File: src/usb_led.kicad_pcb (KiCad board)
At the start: 2 copper layers, 22.2 x 11.4 mm, 6 parts, among them J1 HX TYPE-C 6PIN, SW1 BTN_ON

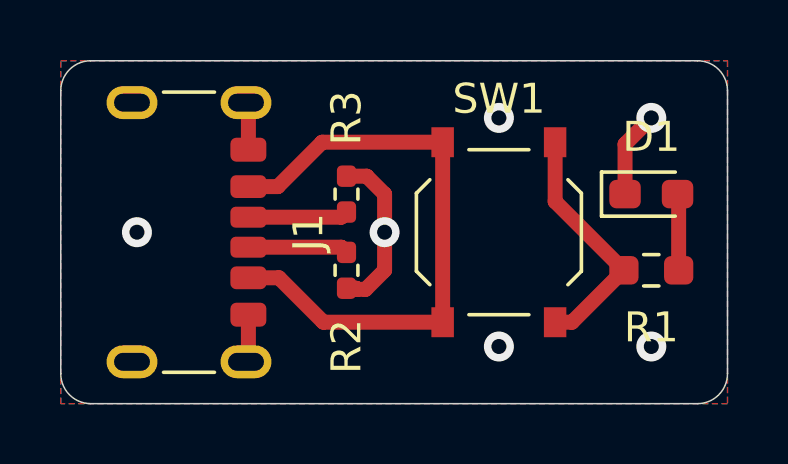
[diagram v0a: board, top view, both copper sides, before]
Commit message: docs: add JLCPCB plugin documentation
Add usage of Bouni's KiCAD JLCPCB tools plugin to README file.

Add PCB copper traces between important GND pads.

Add final PCB 3D render image to README file.
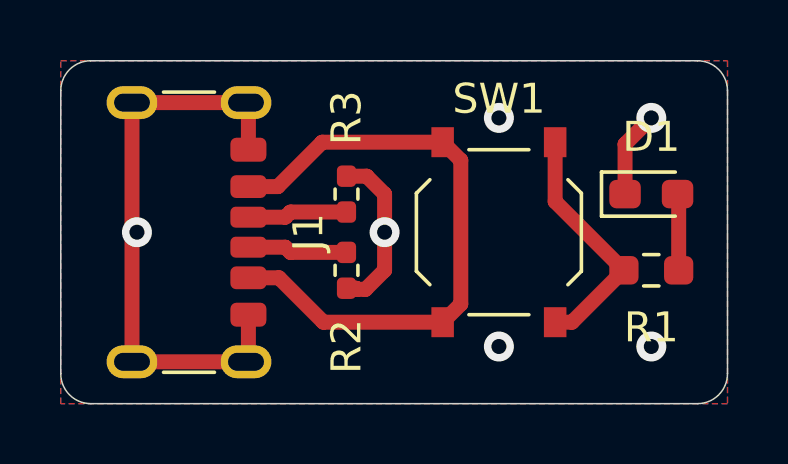
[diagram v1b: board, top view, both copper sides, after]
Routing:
- net GND: track 11.7 -> 28.1 mm
- net Net-(J1-VBUS-PadA9): track 20.2 -> 20.7 mm
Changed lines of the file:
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@@
+	)
+	(segment
+		(start 141.44 91.605)
+		(end 141.605 91.44)
+		(width 0.5)
+		(layer "F.Cu")
+		(net 1)
+	)
+	(segment
+		(start 141.44 95.76)
+		(end 141.44 91.605)
+		(width 0.5)
+		(layer "F.Cu")
+		(net 1)
 	)
 	(segment
@@
 	)
 	(segment
+		(start 141.44 95.76)
+		(end 145.24 95.76)
+		(width 0.5)
+		(layer "F.Cu")
+		(net 1)
+	)
+	(segment
 		(start 145.32 95.68)
 		(end 145.24 95.76)
@@
 	)
 	(segment
+		(start 141.44 91.275)
+		(end 141.605 91.44)
+		(width 0.5)
+		(layer "F.Cu")
+		(net 1)
+	)
+	(segment
 		(start 149.86 90.17)
 		(end 149.86 91.44)
@@
 	)
 	(segment
+		(start 141.44 87.12)
+		(end 141.44 91.275)
+		(width 0.5)
+		(layer "F.Cu")
+		(net 1)
+	)
+	(segment
 		(start 157.875 90.17)
 		(end 157.875 88.505)
@@
 		(net 1)
 	)
+	(segment
+		(start 141.44 87.12)
+		(end 145.24 87.12)
+		(width 0.5)
+		(layer "F.Cu")
+		(net 1)
+	)
 	(via
 		(at 153.67 87.63)
@@
 	)
 	(via
+		(at 158.75 95.25)
+		(size 1)
+		(drill 0.5)
+		(layers "F.Cu" "B.Cu")
+		(free yes)
+		(net 1)
+	)
+	(via
 		(at 141.605 91.44)
 		(size 1)
 		(drill 0.5)
 		(layers "F.Cu" "B.Cu")
-		(free yes)
-		(net 1)
-	)
-	(via
-		(at 158.75 95.25)
-		(size 1)
-		(drill 0.5)
-		(layers "F.Cu" "B.Cu")
-		(free yes)
 		(net 1)
 	)
@@
 	)
 	(segment
+		(start 152.4 93.835)
+		(end 151.795 94.44)
+		(width 0.5)
+		(layer "F.Cu")
+		(net 3)
+	)
+	(segment
 		(start 147.820741 94.44)
 		(end 151.795 94.44)
@@
 	)
 	(segment
+		(start 151.795 88.44)
+		(end 152.4 89.045)
+		(width 0.5)
+		(layer "F.Cu")
+		(net 3)
+	)
+	(segment
+		(start 152.4 89.045)
+		(end 152.4 93.835)
+		(width 0.5)
+		(layer "F.Cu")
+		(net 3)
+	)
+	(segment
 		(start 145.32 89.92)
 		(end 146.3 89.92)
@@
 	)
 	(segment
-		(start 151.795 88.44)
-		(end 151.795 94.44)
-		(width 0.5)
-		(layer "F.Cu")
-		(net 3)
-	)
-	(segment
 		(start 145.32 90.94)
-		(end 148.4175 90.94)
+		(end 146.55 90.94)
 		(width 0.5)
 		(layer "F.Cu")
@@
 	)
 	(segment
-		(start 148.4175 90.94)
+		(start 146.55 90.94)
+		(end 146.7225 90.7675)
+		(width 0.5)
+		(layer "F.Cu")
+		(net 4)
+	)
+	(segment
+		(start 146.7225 90.7675)
 		(end 148.59 90.7675)
 		(width 0.5)
@@
 	)
 	(segment
-		(start 148.4175 91.94)
+		(start 145.32 91.94)
+		(end 146.55 91.94)
+		(width 0.5)
+		(layer "F.Cu")
+		(net 5)
+	)
+	(segment
+		(start 146.7225 92.1125)
 		(end 148.59 92.1125)
 		(width 0.5)
@@
 	)
 	(segment
-		(start 145.32 91.94)
-		(end 148.4175 91.94)
-		(width 0.5)
-		(layer "F.Cu")
+		(start 146.55 91.94)
+		(end 146.7225 92.1125)
+		(width 0.5)
+		(layer "F.Cu")
